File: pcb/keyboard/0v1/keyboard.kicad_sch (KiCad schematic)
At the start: 140 parts, among them SW1 A, SW10 A, SW11 A, SW12 A, SW13 A, SW14 A, SW15 A, SW16 A, SW17 A, SW18 A, SW19 A, SW2 A, SW20 A, SW21 A, SW22 A, SW23 A, SW24 A, SW25 A, SW26 A, SW27 A, SW28 A, SW29 A, SW3 A, SW30 A, SW31 A, SW32 A, SW33 A, SW34 A, SW35 A, SW36 A, SW37 A, SW38 A, SW39 A, SW4 A, SW40 A, SW41 A, SW42 A, SW43 A, SW44 A, SW45 A, SW46 A, SW47 A, SW48 A, SW49 A, SW5 A, SW50 A, SW51 A, SW52 A, SW53 A, SW54 A, SW55 A, SW56 A, SW57 A, SW58 A, SW59 A, SW6 A, SW60 A, SW61 A, SW62 A, SW63 A, SW7 A, SW8 A, SW9 A, U1 MDBT50Q-P1MV2, Y1 32.768

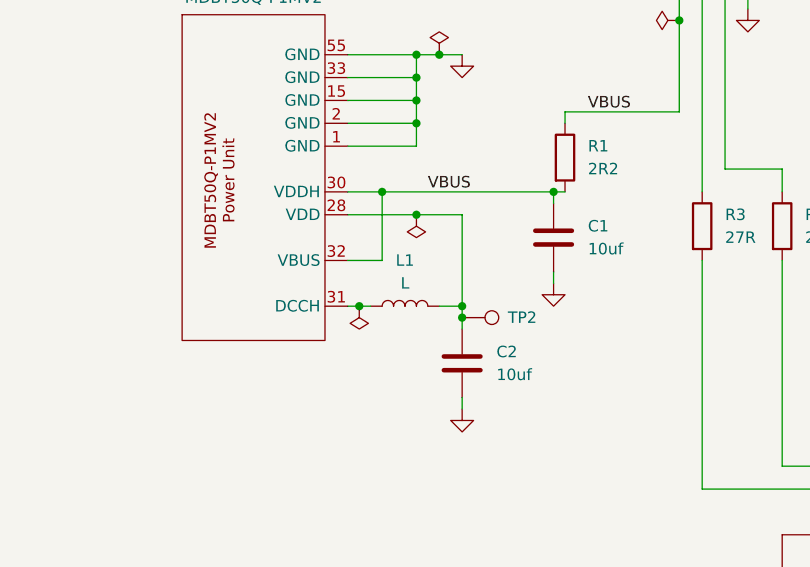
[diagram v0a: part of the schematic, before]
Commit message: Fix missing label for l1 inductor
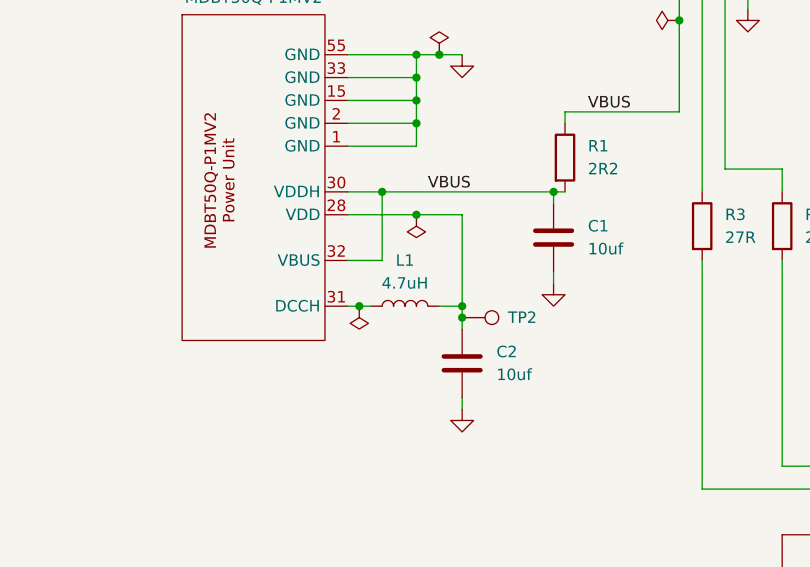
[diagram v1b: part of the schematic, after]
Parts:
- L1: value L -> 4.7uH
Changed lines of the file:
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@@
 			)
 		)
-		(property "Value" "L"
+		(property "Value" "4.7uH"
 			(at 443.23 71.12 90)
 			(effects
